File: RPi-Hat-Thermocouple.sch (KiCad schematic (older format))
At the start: 28 parts, among them J1 RPi_GPIO, J2 Push Terminal, J3 Push Terminal, J4 Push Terminal, SW1 Write, U1 AT24CS32, U2 MAX31855, U3 MAX31855, U4 MAX31855, U5 74LVC139, U6 DS18S20, U7 DS3231M

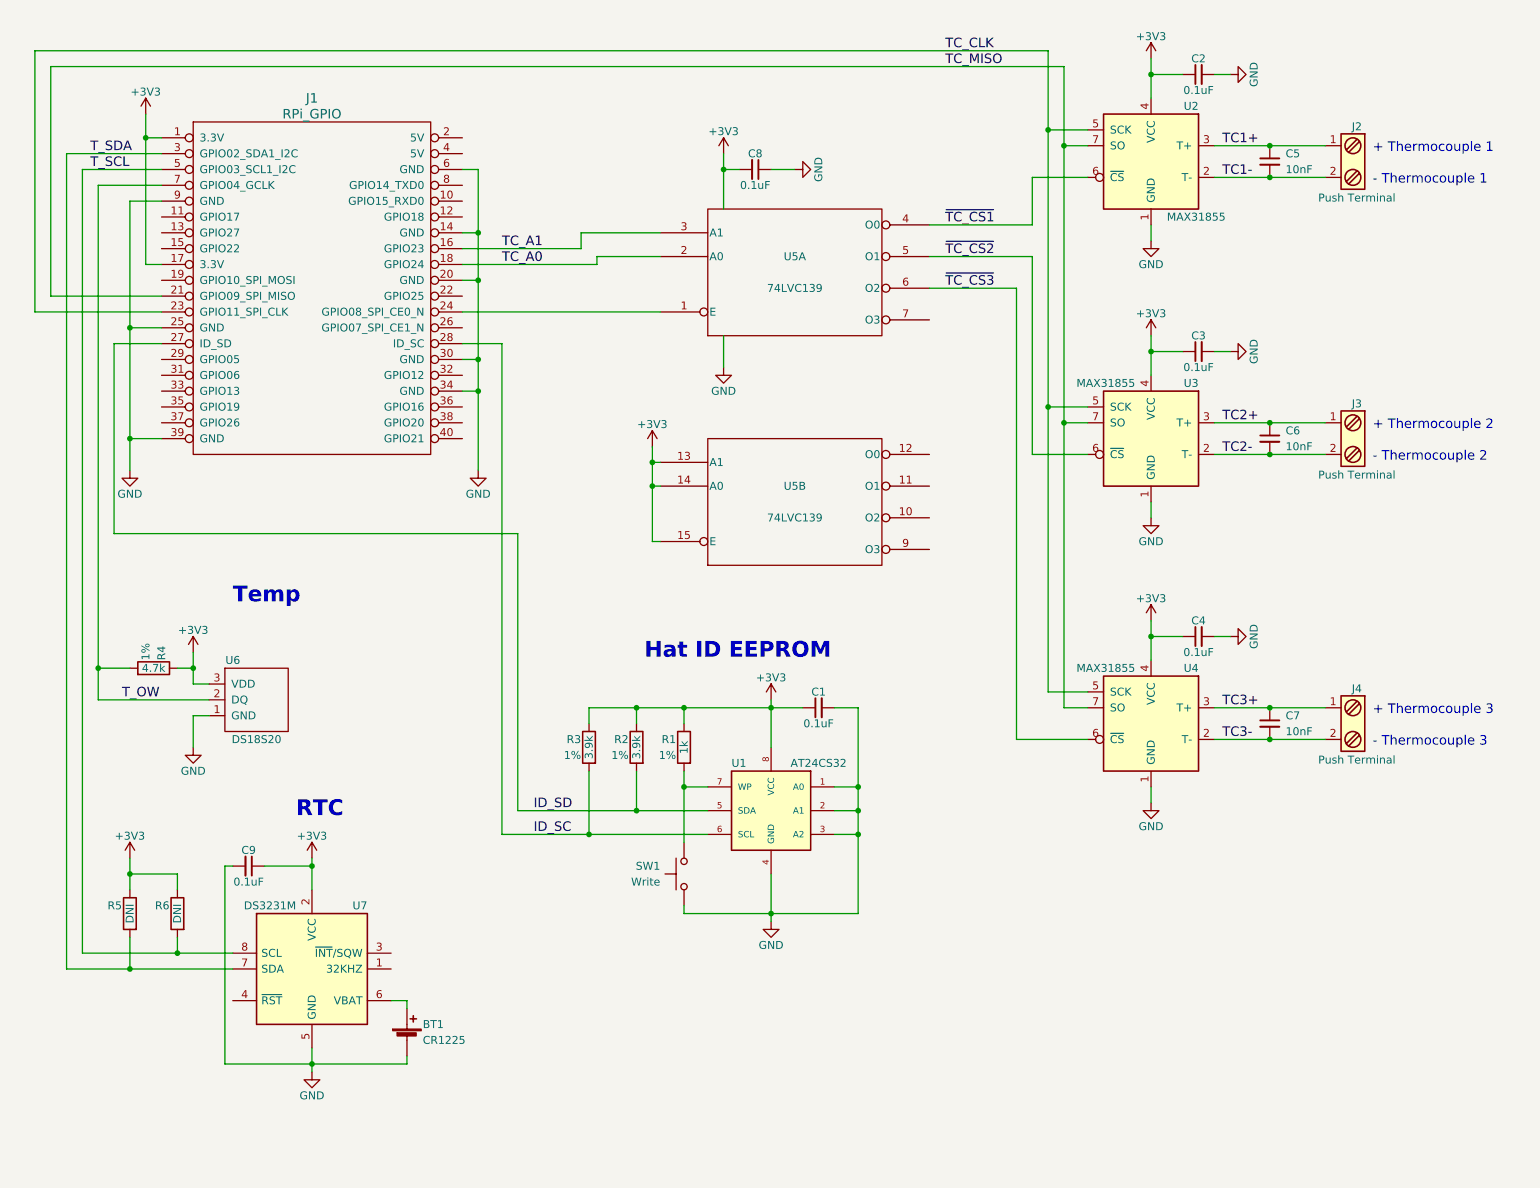
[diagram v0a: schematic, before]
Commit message: Added Alert Buzzer.
Rev 1.1 will be released soon.
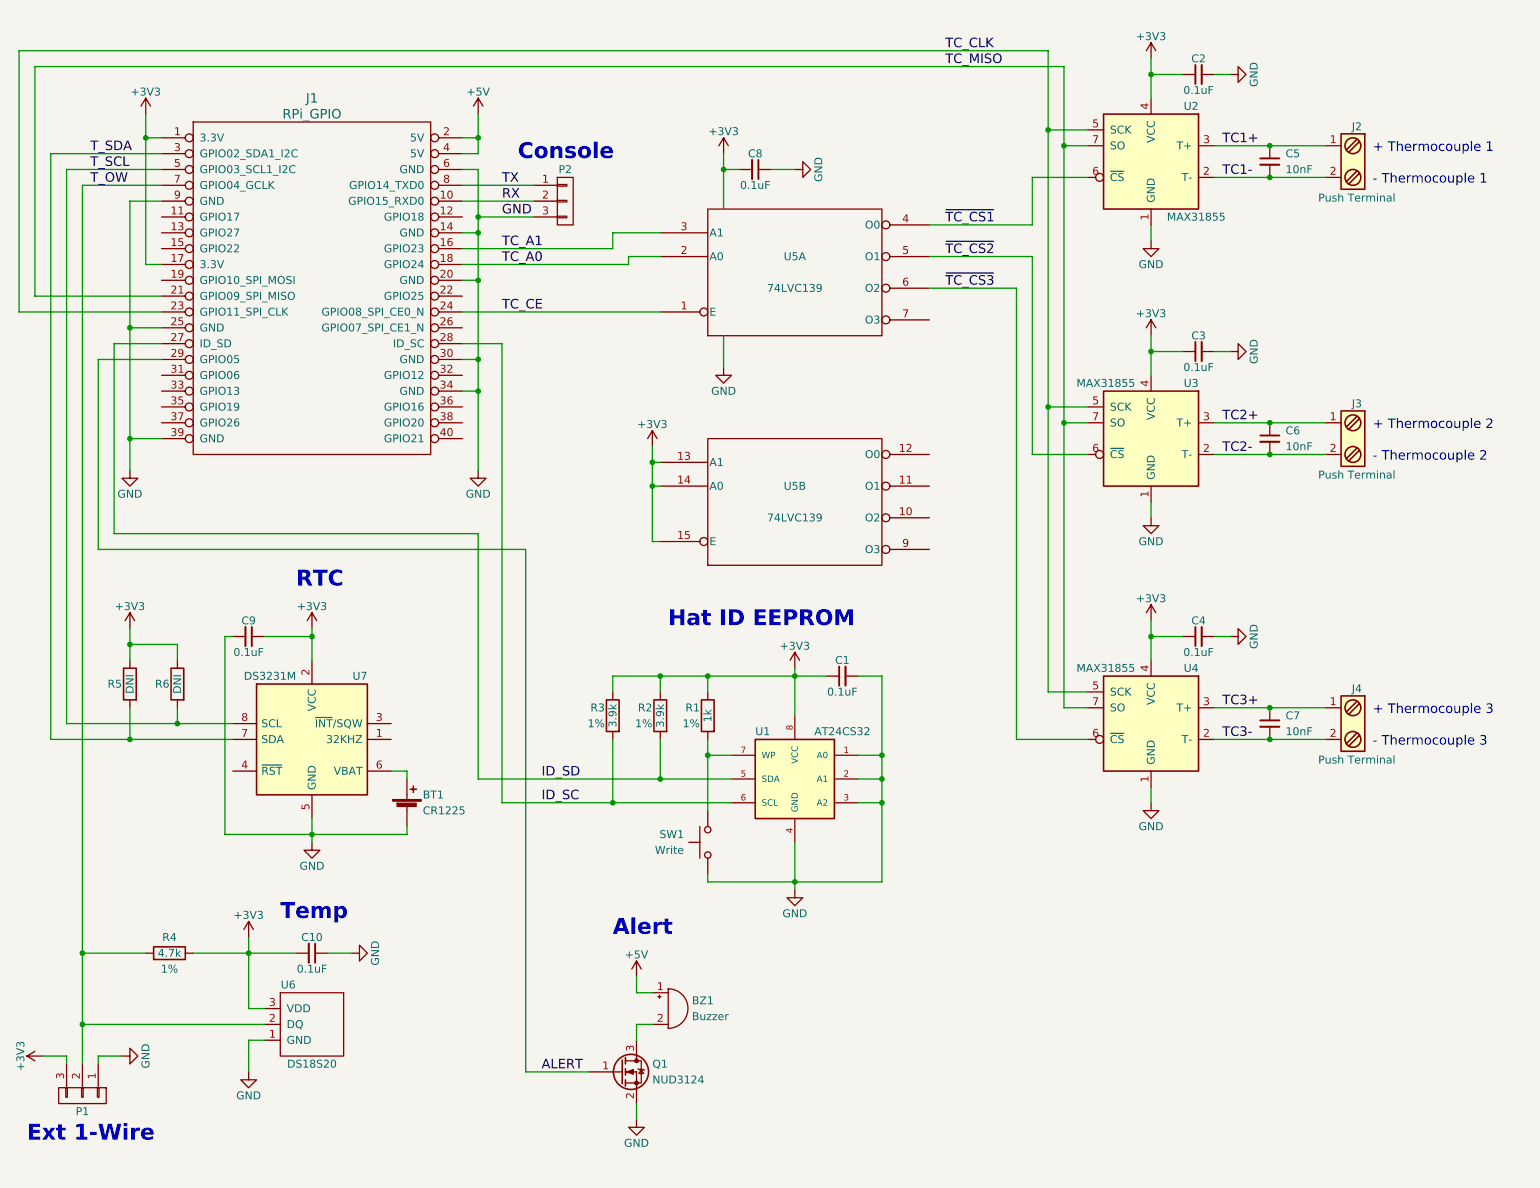
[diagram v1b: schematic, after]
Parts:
- added BZ1: Buzzer, cui-ml:CMI-9655S-SMT, symbol Buzzer
- added C10: 0.1uF, Capacitors_SMD:C_0603, symbol C_Small
- added P1: CONN_01X03, Pin_Headers:Pin_Header_Straight_1x03_Pitch2.00mm, symbol CONN_01X03
- added P2: CONN_01X03, Pin_Headers:Pin_Header_Straight_1x03_Pitch2.54mm, symbol CONN_01X03
- added Q1: NUD3124, TO_SOT_Packages_SMD:SOT-23, symbol NUD3124
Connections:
- net +3V3: now also C10.2, P1.3 (P3)
- net GND: now also C10.1, P1.1 (P1), P2.3 (P3), Q1.2 (S)
- net T_OW: now also P1.2 (P2)
- net RX: now reaches J1.10 (GPIO15_RXD0)
- net RX: now also P2.2 (P2)
- net +5V: now reaches J1.2 (5V)
- net +5V: now also J1.4 (5V), BZ1.1 (-)
- net TC_CE: now reaches J1.24 (GPIO08_SPI_CE0_N), U5.1 (E)
- net ALERT: now reaches J1.29 (GPIO05)
- net ALERT: now also Q1.1 (G)
- net TX: now reaches J1.8 (GPIO14_TXD0)
- net TX: now also P2.1 (P1)
- new net: BZ1.2 (+), Q1.3 (D)
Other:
- note added: "Alert"
- note added: "Console"
- note added: "Ext 1-Wire"
- moved on the sheet: BT1, C1, C9, R1, R2, R3, R4, R5, R6, SW1, U1, U6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

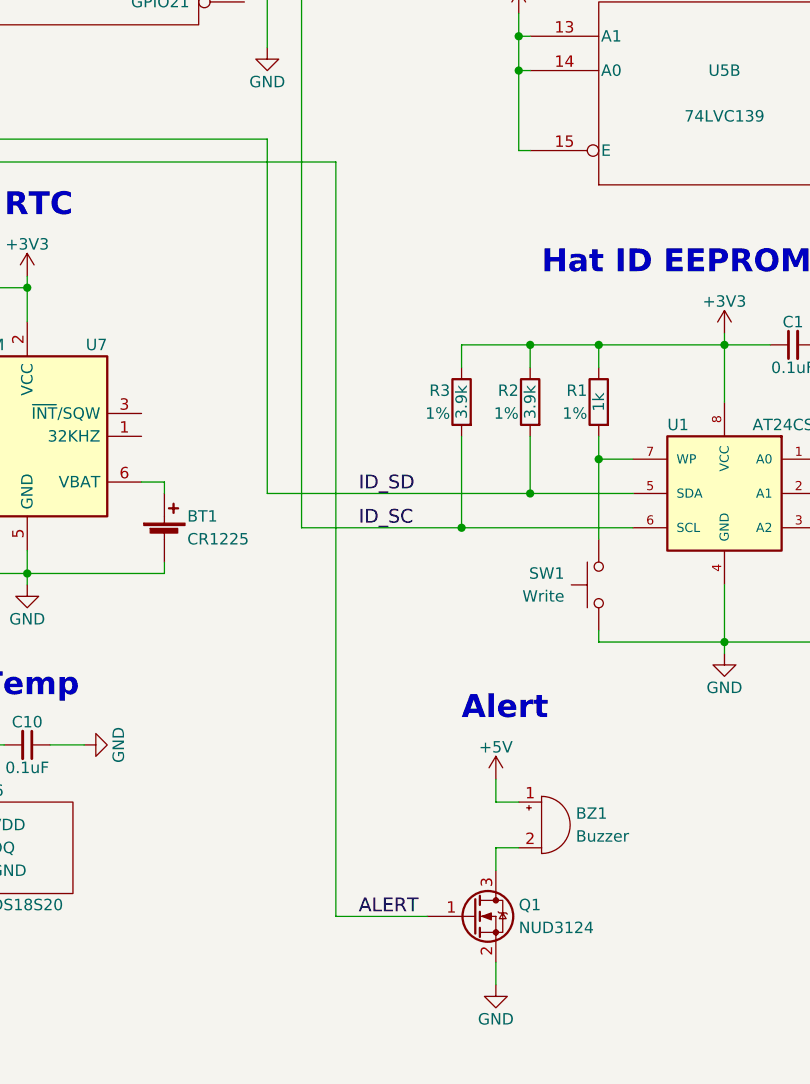
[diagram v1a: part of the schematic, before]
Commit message: Add R7
R7 prevents alert from going off until software
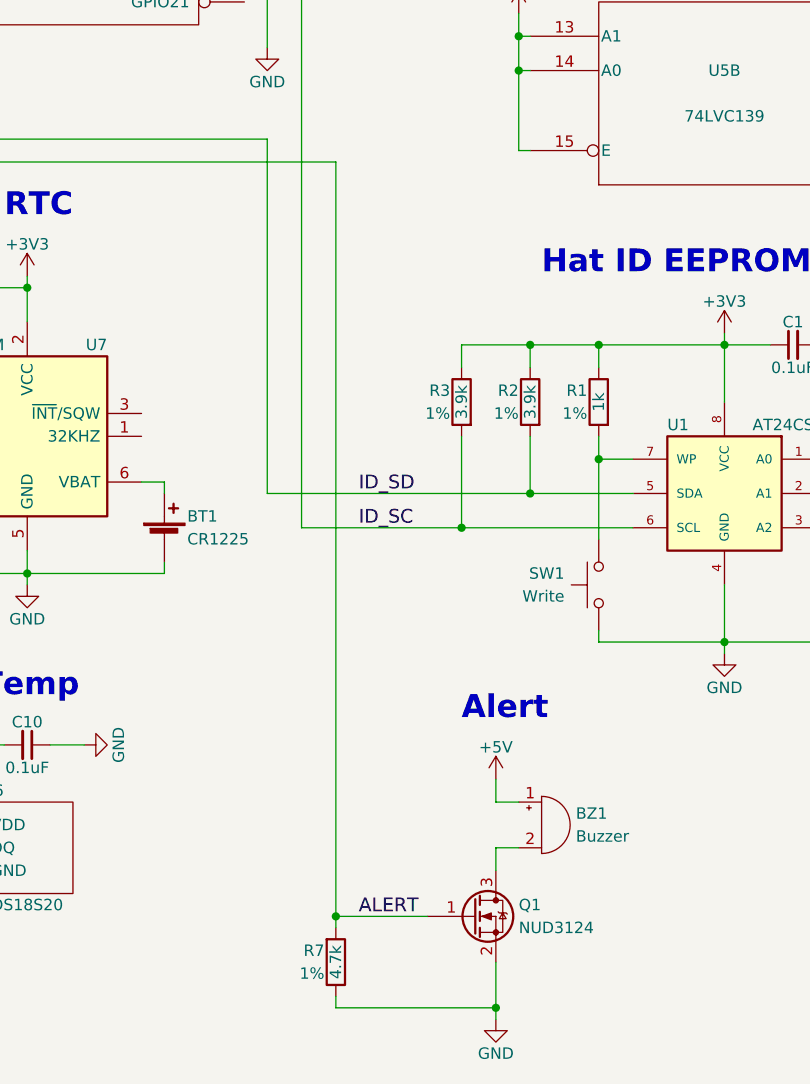
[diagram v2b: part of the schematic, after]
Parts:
- added R7: 4.7k, Resistors_SMD:R_0603, symbol R
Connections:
- net ALERT: now also R7.2
- net GND: now also R7.1
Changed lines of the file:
@@
 Title "Raspberry Pi Thermocouple Hat"
 Date "March 2017"
-Rev "1.1"
+Rev "1.2"
 Comp "Mike Lawrence"
 Comment1 "Rev 1.1 Added Alert, Ext 1-Wire connections, and console connections."
-Comment2 ""
+Comment2 "Rev 1.2 Added R7 to prevent Alert from activating on power on."
 Comment3 ""
 Comment4 ""
@@
 $EndComp
 $Comp
-L GND #PWR01
+L GND #PWR22
 U 1 1 58A9C6BD
 P 5750 6200
-F 0 "#PWR01" H 5750 5950 50  0001 C CNN
+F 0 "#PWR22" H 5750 5950 50  0001 C CNN
 F 1 "GND" H 5750 6050 50  0000 C CNN
 F 2 "" H 5750 6200 50  0000 C CNN
@@
 $EndComp
 $Comp
-L +3V3 #PWR02
+L +3V3 #PWR19
 U 1 1 58A9E27B
 P 5750 4800
-F 0 "#PWR02" H 5750 4650 50  0001 C CNN
+F 0 "#PWR19" H 5750 4650 50  0001 C CNN
 F 1 "+3V3" H 5750 4940 50  0000 C CNN
 F 2 "" H 5750 4800 50  0000 C CNN
@@
 $EndComp
 $Comp
-L GND #PWR03
+L GND #PWR7
 U 1 1 58AA0BFC
 P 8000 2100
-F 0 "#PWR03" H 8000 1850 50  0001 C CNN
+F 0 "#PWR7" H 8000 1850 50  0001 C CNN
 F 1 "GND" H 8000 1950 50  0000 C CNN
 F 2 "" H 8000 2100 50  0000 C CNN
@@
 $EndComp
 $Comp
-L +3V3 #PWR04
+L +3V3 #PWR1
 U 1 1 58AA0C37
 P 8000 950
-F 0 "#PWR04" H 8000 800 50  0001 C CNN
+F 0 "#PWR1" H 8000 800 50  0001 C CNN
 F 1 "+3V3" H 8000 1090 50  0000 C CNN
 F 2 "" H 8000 950 50  0000 C CNN
@@
 $EndComp
 $Comp
-L GND #PWR05
+L GND #PWR2
 U 1 1 58AA0CAF
 P 8500 1050
-F 0 "#PWR05" H 8500 800 50  0001 C CNN
+F 0 "#PWR2" H 8500 800 50  0001 C CNN
 F 1 "GND" H 8500 900 50  0000 C CNN
 F 2 "" H 8500 1050 50  0000 C CNN
@@
 $EndComp
 $Comp
-L GND #PWR06
+L GND #PWR14
 U 1 1 58AA14BB
 P 8000 3850
-F 0 "#PWR06" H 8000 3600 50  0001 C CNN
+F 0 "#PWR14" H 8000 3600 50  0001 C CNN
 F 1 "GND" H 8000 3700 50  0000 C CNN
 F 2 "" H 8000 3850 50  0000 C CNN
@@
 $EndComp
 $Comp
-L +3V3 #PWR07
+L +3V3 #PWR8
 U 1 1 58AA14C1
 P 8000 2700
-F 0 "#PWR07" H 8000 2550 50  0001 C CNN
+F 0 "#PWR8" H 8000 2550 50  0001 C CNN
 F 1 "+3V3" H 8000 2840 50  0000 C CNN
 F 2 "" H 8000 2700 50  0000 C CNN
@@
 $EndComp
 $Comp
-L GND #PWR08
+L GND #PWR9
 U 1 1 58AA14C7
 P 8500 2800
-F 0 "#PWR08" H 8500 2550 50  0001 C CNN
+F 0 "#PWR9" H 8500 2550 50  0001 C CNN
 F 1 "GND" H 8500 2650 50  0000 C CNN
 F 2 "" H 8500 2800 50  0000 C CNN
@@
 $EndComp
 $Comp
-L GND #PWR09
+L GND #PWR20
 U 1 1 58AA15AA
 P 8000 5650
-F 0 "#PWR09" H 8000 5400 50  0001 C CNN
+F 0 "#PWR20" H 8000 5400 50  0001 C CNN
 F 1 "GND" H 8000 5500 50  0000 C CNN
 F 2 "" H 8000 5650 50  0000 C CNN
@@
 $EndComp
 $Comp
-L +3V3 #PWR010
+L +3V3 #PWR15
 U 1 1 58AA15B0
 P 8000 4500
-F 0 "#PWR010" H 8000 4350 50  0001 C CNN
+F 0 "#PWR15" H 8000 4350 50  0001 C CNN
 F 1 "+3V3" H 8000 4640 50  0000 C CNN
 F 2 "" H 8000 4500 50  0000 C CNN
@@
 $EndComp
 $Comp
-L GND #PWR011
+L GND #PWR18
 U 1 1 58AA15B6
 P 8500 4600
-F 0 "#PWR011" H 8500 4350 50  0001 C CNN
+F 0 "#PWR18" H 8500 4350 50  0001 C CNN
 F 1 "GND" H 8500 4450 50  0000 C CNN
 F 2 "" H 8500 4600 50  0000 C CNN
@@
 - Thermocouple 3
 $Comp
-L +3V3 #PWR012
+L +3V3 #PWR3
 U 1 1 58AA1D76
 P 1650 1300
-F 0 "#PWR012" H 1650 1150 50  0001 C CNN
+F 0 "#PWR3" H 1650 1150 50  0001 C CNN
 F 1 "+3V3" H 1650 1440 50  0000 C CNN
 F 2 "" H 1650 1300 50  0000 C CNN
@@
 $EndComp
 $Comp
-L GND #PWR013
+L GND #PWR13
 U 1 1 58AA2E66
 P 3750 3550
-F 0 "#PWR013" H 3750 3300 50  0001 C CNN
+F 0 "#PWR13" H 3750 3300 50  0001 C CNN
 F 1 "GND" H 3750 3400 50  0000 C CNN
 F 2 "" H 3750 3550 50  0000 C CNN
@@
 $EndComp
 $Comp
-L GND #PWR014
+L GND #PWR12
 U 1 1 58AA2EAA
 P 1550 3550
-F 0 "#PWR014" H 1550 3300 50  0001 C CNN
+F 0 "#PWR12" H 1550 3300 50  0001 C CNN
 F 1 "GND" H 1550 3400 50  0000 C CNN
 F 2 "" H 1550 3550 50  0000 C CNN
@@
 $EndComp
 $Comp
-L +3V3 #PWR015
+L +3V3 #PWR11
 U 1 1 58ADE093
 P 4850 3400
-F 0 "#PWR015" H 4850 3250 50  0001 C CNN
+F 0 "#PWR11" H 4850 3250 50  0001 C CNN
 F 1 "+3V3" H 4850 3540 50  0000 C CNN
 F 2 "" H 4850 3400 50  0000 C CNN
@@
 $EndComp
 $Comp
-L +3V3 #PWR016
+L +3V3 #PWR5
 U 1 1 58ADEFE7
 P 5300 1550
-F 0 "#PWR016" H 5300 1400 50  0001 C CNN
+F 0 "#PWR5" H 5300 1400 50  0001 C CNN
 F 1 "+3V3" H 5300 1690 50  0000 C CNN
 F 2 "" H 5300 1550 50  0000 C CNN
@@
 $EndComp
 $Comp
-L GND #PWR017
+L GND #PWR10
 U 1 1 58ADF0BC
 P 5300 2900
-F 0 "#PWR017" H 5300 2650 50  0001 C CNN
+F 0 "#PWR10" H 5300 2650 50  0001 C CNN
 F 1 "GND" H 5300 2750 50  0000 C CNN
 F 2 "" H 5300 2900 50  0000 C CNN
@@
 $EndComp
 $Comp
-L GND #PWR018
+L GND #PWR6
 U 1 1 58AE1194
 P 5750 1650
-F 0 "#PWR018" H 5750 1400 50  0001 C CNN
+F 0 "#PWR6" H 5750 1400 50  0001 C CNN
 F 1 "GND" H 5750 1500 50  0000 C CNN
 F 2 "" H 5750 1650 50  0000 C CNN
@@
 $EndComp
 $Comp
-L GND #PWR019
+L GND #PWR21
 U 1 1 58B05713
 P 2700 5900
-F 0 "#PWR019" H 2700 5650 50  0001 C CNN
+F 0 "#PWR21" H 2700 5650 50  0001 C CNN
 F 1 "GND" H 2700 5750 50  0000 C CNN
 F 2 "" H 2700 5900 50  0000 C CNN
@@
 $EndComp
 $Comp
-L +3V3 #PWR020
+L +3V3 #PWR17
 U 1 1 58B05F55
 P 2700 4550
-F 0 "#PWR020" H 2700 4400 50  0001 C CNN
+F 0 "#PWR17" H 2700 4400 50  0001 C CNN
 F 1 "+3V3" H 2700 4690 50  0000 C CNN
 F 2 "" H 2700 4550 50  0000 C CNN
@@
 Temp
 $Comp
-L +3V3 #PWR021
+L +3V3 #PWR23
 U 1 1 58B06FC2
 P 2300 6500
-F 0 "#PWR021" H 2300 6350 50  0001 C CNN
+F 0 "#PWR23" H 2300 6350 50  0001 C CNN
 F 1 "+3V3" H 2300 6640 50  0000 C CNN
 F 2 "" H 2300 6500 50  0000 C CNN
@@
 $EndComp
 $Comp
-L GND #PWR022
+L GND #PWR28
 U 1 1 58B07074
 P 2300 7350
-F 0 "#PWR022" H 2300 7100 50  0001 C CNN
+F 0 "#PWR28" H 2300 7100 50  0001 C CNN
 F 1 "GND" H 2300 7200 50  0000 C CNN
 F 2 "" H 2300 7350 50  0000 C CNN
@@
 TC_CLK
 $Comp
-L +3V3 #PWR023
+L +3V3 #PWR16
 U 1 1 58B0D3B6
 P 1550 4550
-F 0 "#PWR023" H 1550 4400 50  0001 C CNN
+F 0 "#PWR16" H 1550 4400 50  0001 C CNN
 F 1 "+3V3" H 1550 4690 50  0000 C CNN
 F 2 "" H 1550 4550 50  0000 C CNN
@@
 $EndComp
 $Comp
-L +5V #PWR024
+L +5V #PWR4
 U 1 1 58C3BCED
 P 3750 1300
-F 0 "#PWR024" H 3750 1150 50  0001 C CNN
+F 0 "#PWR4" H 3750 1150 50  0001 C CNN
 F 1 "+5V" H 3750 1440 50  0000 C CNN
 F 2 "" H 3750 1300 50  0000 C CNN
@@
 $EndComp
 $Comp
-L +5V #PWR025
+L +5V #PWR25
 U 1 1 58C460AE
 P 4750 6750
-F 0 "#PWR025" H 4750 6600 50  0001 C CNN
+F 0 "#PWR25" H 4750 6600 50  0001 C CNN
 F 1 "+5V" H 4750 6890 50  0000 C CNN
 F 2 "" H 4750 6750 50  0000 C CNN
@@
 $EndComp
 $Comp
-L GND #PWR026
+L GND #PWR29
 U 1 1 58C4617D
-P 4750 7650
-F 0 "#PWR026" H 4750 7400 50  0001 C CNN
-F 1 "GND" H 4750 7500 50  0000 C CNN
-F 2 "" H 4750 7650 50  0000 C CNN
-F 3 "" H 4750 7650 50  0000 C CNN
-	1    4750 7650
+P 4750 7800
+F 0 "#PWR29" H 4750 7550 50  0001 C CNN
+F 1 "GND" H 4750 7650 50  0000 C CNN
+F 2 "" H 4750 7800 50  0000 C CNN
+F 3 "" H 4750 7800 50  0000 C CNN
+	1    4750 7800
 	1    0    0    -1
 $EndComp
@@
 $EndComp
 $Comp
-L GND #PWR027
+L GND #PWR24
 U 1 1 58C47897
 P 2950 6600
-F 0 "#PWR027" H 2950 6350 50  0001 C CNN
+F 0 "#PWR24" H 2950 6350 50  0001 C CNN
 F 1 "GND" H 2950 6450 50  0000 C CNN
 F 2 "" H 2950 6600 50  0000 C CNN
@@
 $EndComp
 $Comp
-L GND #PWR028
+L GND #PWR27
 U 1 1 58C4A2EC
 P 1500 7250
-F 0 "#PWR028" H 1500 7000 50  0001 C CNN
+F 0 "#PWR27" H 1500 7000 50  0001 C CNN
 F 1 "GND" H 1500 7100 50  0000 C CNN
 F 2 "" H 1500 7250 50  0000 C CNN
@@
 $EndComp
 $Comp
-L +3V3 #PWR029
+L +3V3 #PWR26
 U 1 1 58C4A35A
 P 1000 7250
-F 0 "#PWR029" H 1000 7100 50  0001 C CNN
+F 0 "#PWR26" H 1000 7100 50  0001 C CNN
 F 1 "+3V3" H 1000 7390 50  0000 C CNN
 F 2 "" H 1000 7250 50  0000 C CNN
@@
 	4750 6850 4750 6750
 Wire Wire Line
-	4750 7550 4750 7650
+	4750 7550 4750 7800
 Wire Wire Line
 	4450 7350 4050 7350
 Wire Wire Line
-	4050 7350 4050 4050
+	4050 4050 4050 7400
 Wire Wire Line
 	4050 4050 1350 4050
@@
 Text Label 3900 2550 0    60   ~ 0
 TC_CE
+$Comp
+L R R7
+U 1 1 58D090D7
+P 4050 7550
+F 0 "R7" H 4000 7500 50  0000 R CNN
+F 1 "4.7k" V 4050 7550 50  0000 C CNN
+F 2 "Resistors_SMD:R_0603" V 3980 7550 50  0001 C CNN
+F 3 "https://industrial.panasonic.com/cdbs/www-data/pdf/RDA0000/AOA0000C283.pdf" V 4050 7550 50  0001 C CNN
+F 4 "ERJ-3EKF4701V" H 4050 7550 60  0001 C CNN "Part Number"
+F 5 "Panasonic" H 4050 7550 60  0001 C CNN "Manufacturer"
+F 6 "Mouser" H 4050 7550 60  0001 C CNN "Vendor"
+F 7 "667-ERJ-3EKF4701V" H 4050 7550 60  0001 C CNN "Vendor Part Number"
+F 8 "1%" H 4000 7600 50  0000 R CNN "Tolerance"
+	1    4050 7550
+	1    0    0    1
+$EndComp
+Connection ~ 4050 7350
+Wire Wire Line
+	4050 7700 4050 7750
+Wire Wire Line
+	4050 7750 4750 7750
+Connection ~ 4750 7750
 $EndSCHEMATC

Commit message: Added Analog Power LDO regulator
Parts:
- added C11, C12: 2.2uF, Capacitors_SMD:C_0805, symbol C_Small
- added C13, C14, C15: 10nF, Capacitors_SMD:C_0603, symbol C_Small
- added U8: MCP1754ST, TO_SOT_Packages_SMD:SOT89-3_Housing, symbol MCP1754ST-3302E/MB
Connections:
- net +3V3: no longer C10.2, C2.1, C3.1, C4.1, P1.3 (P3), R4.1, U2.4 (VCC), U3.4 (VCC), U4.4 (VCC), U6.3 (VDD)
- net +5V: now also C12.1, U8.1 (VI)
- net GND: now also C11.2, C12.2, C13.1, C14.1, C15.1, U8.2 (GND)
- new net +3.3VA: C10.2, C11.1, C13.2, C14.2, C15.2, C2.1, C3.1, C4.1, P1.3 (P3), R4.1, U2.4 (VCC), U3.4 (VCC), U4.4 (VCC), U6.3 (VDD), U8.3 (VO)
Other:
- note added: "+ TC 1"
- note added: "+ TC 2"
- note added: "+ TC 3"
- note added: "- TC 1\n"
- note added: "- TC 2\n"
- note added: "- TC 3\n"
- note added: "Analog Power"
- note removed: "+ Thermocouple 1"
- note removed: "+ Thermocouple 2"
- note removed: "+ Thermocouple 3"
- note removed: "- Thermocouple 1\n"
- note removed: "- Thermocouple 2\n"
- note removed: "- Thermocouple 3"
- moved on the sheet: C2, C3, C4, C6, C7, J3, J4, U3, U4
